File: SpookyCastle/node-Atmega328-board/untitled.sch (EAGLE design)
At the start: 20 parts, among them IC2 MEGA48/88/168-AU, J1 RJ11-6PTH

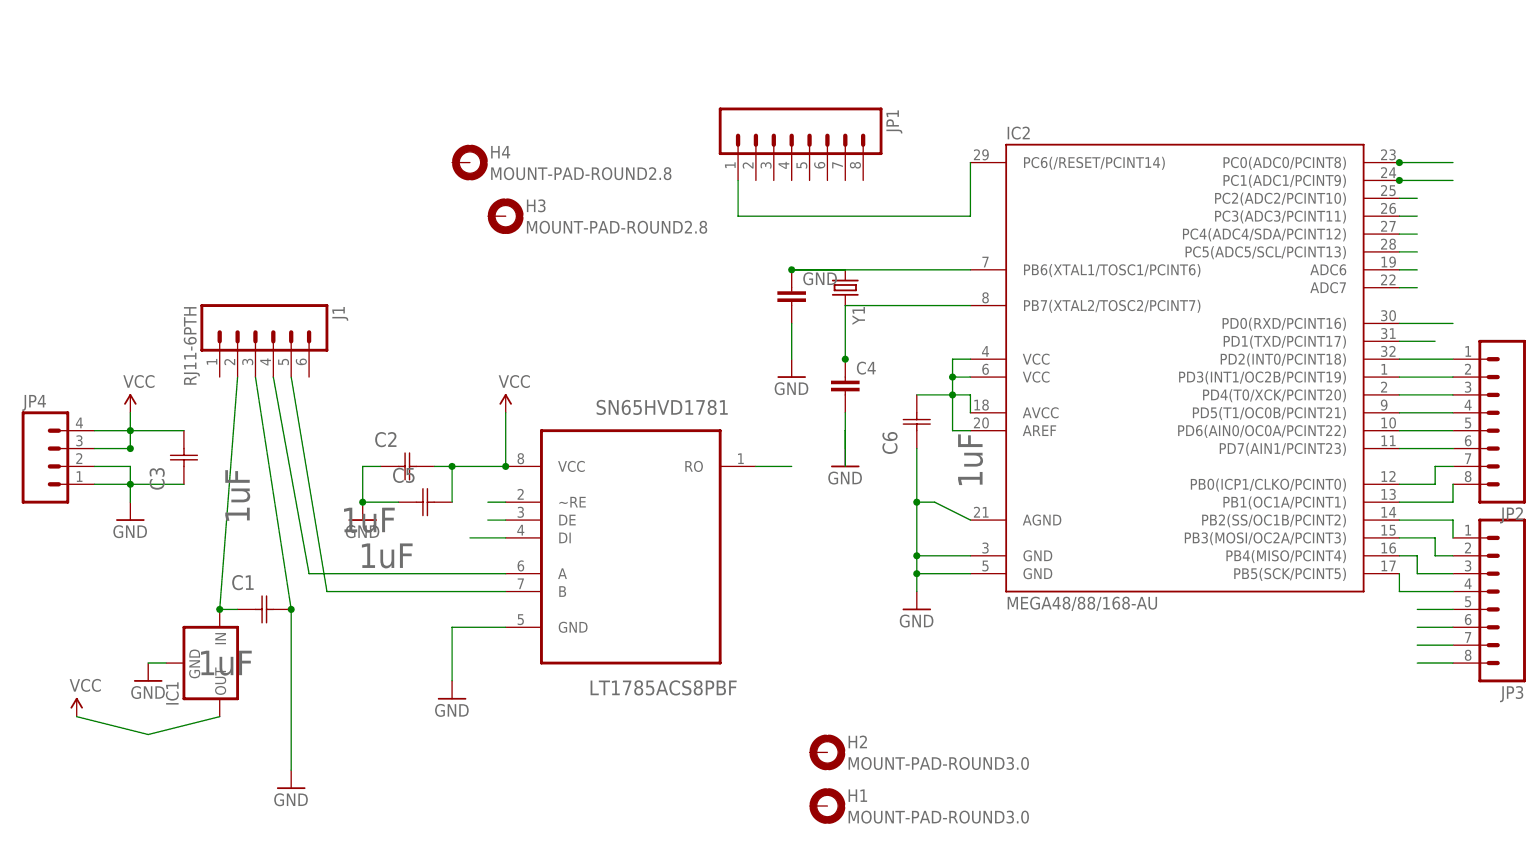
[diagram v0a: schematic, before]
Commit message: Almost finished with the SpookyCastle atmega board, core protocol version 0.7.6: Pin ordering changed for rs485, updated PDF.
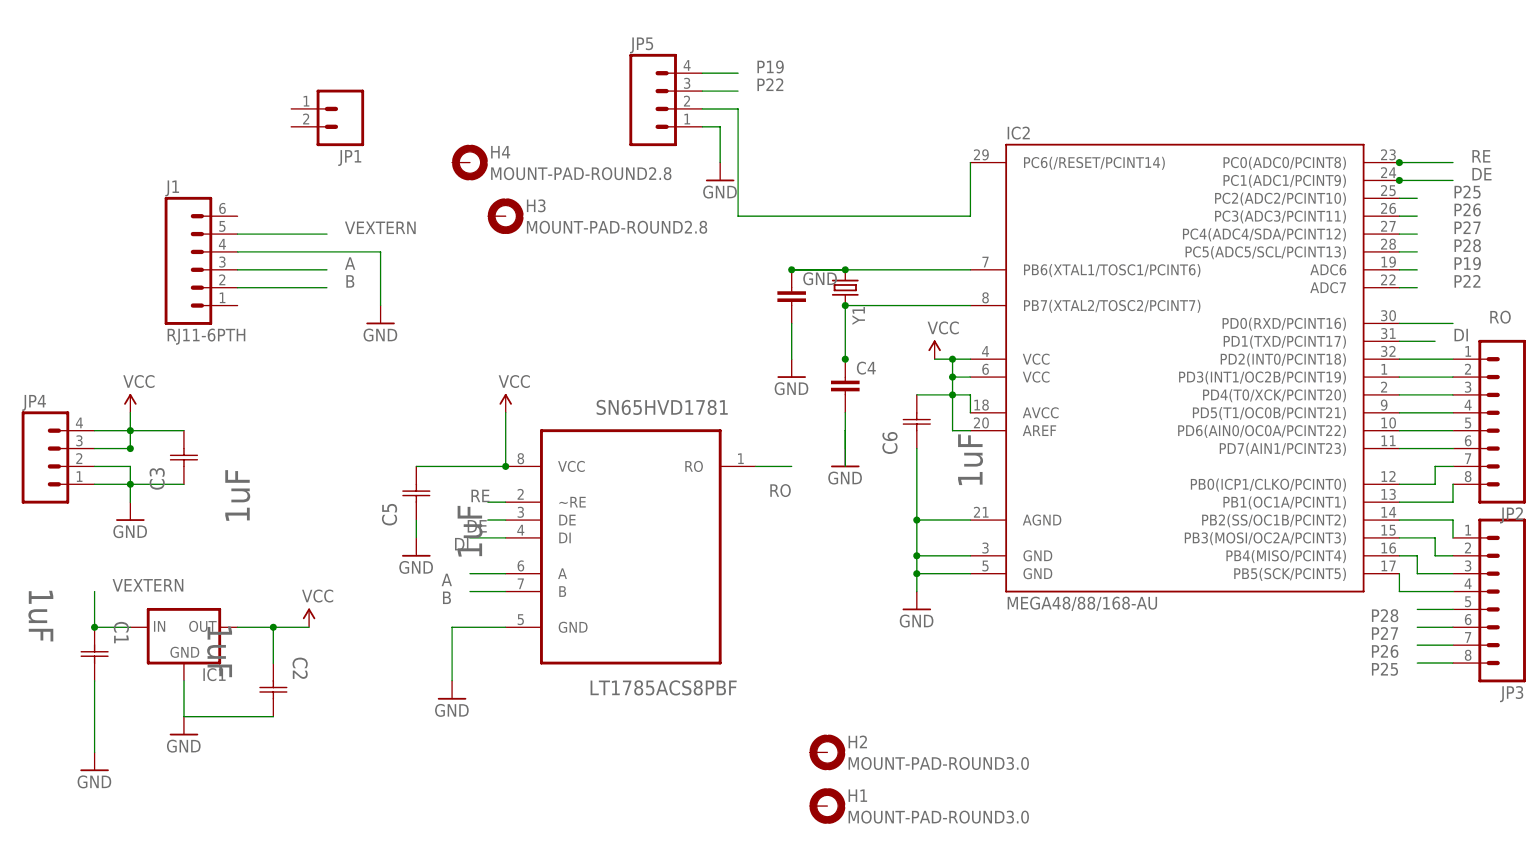
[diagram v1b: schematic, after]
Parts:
- added JP5: (no value), SparkFun - Copy:M04LOCK
- JP1: device SparkFun - Copy:M08LOCK -> SparkFun - Copy:M02PTH
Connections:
- removed net N$1: J1.4, SN65HVD1781.A
- removed net N$2: J1.5, SN65HVD1781.B
- removed net N$3: C1.C1, IC1.IN, J1.2
- new net A: J1.3, SN65HVD1781.A
- new net B: J1.2, SN65HVD1781.B
- new net VEXTERN: C1.C1, IC1.IN, J1.5
- net GND: now also C2.C2, J1.4, JP5.1; no longer C2.C1, J1.3
- net N$22: now also JP5.2; no longer JP1.1
- net P19: now also JP5.4
- net P22: now also JP5.3
- net VCC: now also C2.C1; no longer C2.C2
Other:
- moved on the sheet: C1, C2, C5, IC1, J1

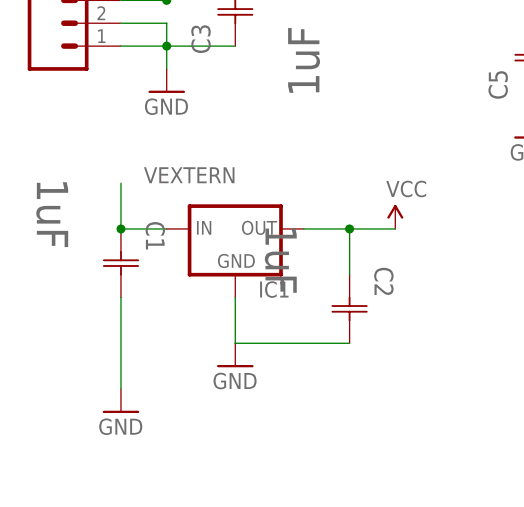
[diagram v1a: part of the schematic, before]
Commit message: Added option for 1210 capacitor on input of vreg, mitered some noise critical routing.
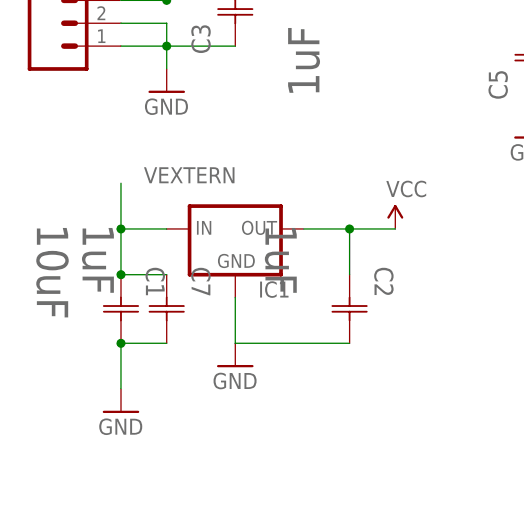
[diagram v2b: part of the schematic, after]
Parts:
- added C7: 1uF, Murata_By_element14_Batch_1:GRM21BR71H105KA12L
- C1: value 1uF -> 10uF; device Murata_By_element14_Batch_1:GRM21BR71H105KA12L -> Murata_By_element14_Batch_1:GRM32ER7YA106KA12L
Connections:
- net GND: now also C7.C2
- net VEXTERN: now also C7.C1
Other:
- moved on the sheet: C1
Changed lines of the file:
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@@
 <part name="GND1" library="SparkFun - Copy" deviceset="GND" device=""/>
 <part name="P+1" library="SparkFun - Copy" deviceset="VCC" device=""/>
-<part name="C1" library="Murata_By_element14_Batch_1" deviceset="GRM21BR71H105KA12L" device="" value="1uF"/>
 <part name="P+2" library="SparkFun - Copy" deviceset="VCC" device=""/>
 <part name="C2" library="Murata_By_element14_Batch_1" deviceset="GRM21BR71H105KA12L" device="" value="1uF"/>
@@
 <part name="JP5" library="SparkFun - Copy" deviceset="M04" device="LOCK"/>
 <part name="GND10" library="SparkFun - Copy" deviceset="GND" device=""/>
+<part name="C1" library="Murata_By_element14_Batch_1" deviceset="GRM32ER7YA106KA12L" device="" value="10uF"/>
+<part name="C7" library="Murata_By_element14_Batch_1" deviceset="GRM21BR71H105KA12L" device="" value="1uF">
+<attribute name="MPN" value="GRM21BR71H105KA12L "/>
+<attribute name="OC_FARNELL" value="1735541"/>
+<attribute name="OC_NEWARK" value="24R6342"/>
+<attribute name="SUPPLIER" value="Murata"/>
+<attribute name="TOLERANCE" value="±10%"/>
+<attribute name="VALUE" value="1uF"/>
+<attribute name="VOLTAGERATING" value="50V"/>
+</part>
 </parts>
 <sheets>
@@
 <instance part="GND1" gate="1" x="-15.24" y="15.24"/>
 <instance part="P+1" gate="1" x="15.24" y="35.56"/>
-<instance part="C1" gate="A" x="-15.24" y="35.56" rot="R270"/>
 <instance part="P+2" gate="1" x="43.18" y="66.04"/>
 <instance part="C2" gate="A" x="10.16" y="30.48" rot="R270"/>
@@
 <instance part="JP5" gate="G$1" x="66.04" y="109.22"/>
 <instance part="GND10" gate="1" x="73.66" y="99.06"/>
+<instance part="C1" gate="A" x="-15.24" y="30.48" rot="R270"/>
+<instance part="C7" gate="A" x="-10.16" y="30.48" rot="R270"/>
 </instances>
 <busses>
@@
 </segment>
 <segment>
-<wire x1="-15.24" y1="27.94" x2="-15.24" y2="17.78" width="0.1524" layer="91"/>
-<pinref part="GND1" gate="1" pin="GND"/>
-<pinref part="C1" gate="A" pin="C2"/>
-</segment>
-<segment>
 <pinref part="C4" gate="G$1" pin="2"/>
 <pinref part="GND4" gate="1" pin="GND"/>
@@
 <pinref part="GND10" gate="1" pin="GND"/>
 </segment>
+<segment>
+<pinref part="GND1" gate="1" pin="GND"/>
+<pinref part="C1" gate="A" pin="C2"/>
+<wire x1="-15.24" y1="17.78" x2="-15.24" y2="22.86" width="0.1524" layer="91"/>
+<pinref part="C7" gate="A" pin="C2"/>
+<wire x1="-10.16" y1="22.86" x2="-15.24" y2="22.86" width="0.1524" layer="91"/>
+<junction x="-15.24" y="22.86"/>
+</segment>
 </net>
 <net name="VEXTERN" class="1">
 <segment>
-<pinref part="C1" gate="A" pin="C1"/>
 <pinref part="IC1" gate="G$1" pin="IN"/>
 <wire x1="-10.16" y1="35.56" x2="-15.24" y2="35.56" width="0.1524" layer="91"/>
-<junction x="-15.24" y="35.56"/>
 <wire x1="-15.24" y1="35.56" x2="-15.24" y2="40.64" width="0.1524" layer="91"/>
 <label x="-12.7" y="40.64" size="1.778" layer="95"/>
-</segment>
-<segment>
+<pinref part="C1" gate="A" pin="C1"/>
+<wire x1="-15.24" y1="30.48" x2="-15.24" y2="35.56" width="0.1524" layer="91"/>
+<junction x="-15.24" y="35.56"/>
+<pinref part="C7" gate="A" pin="C1"/>
+<wire x1="-15.24" y1="30.48" x2="-10.16" y2="30.48" width="0.1524" layer="91"/>
+<junction x="-15.24" y="30.48"/>
+</segment>
+<segment>

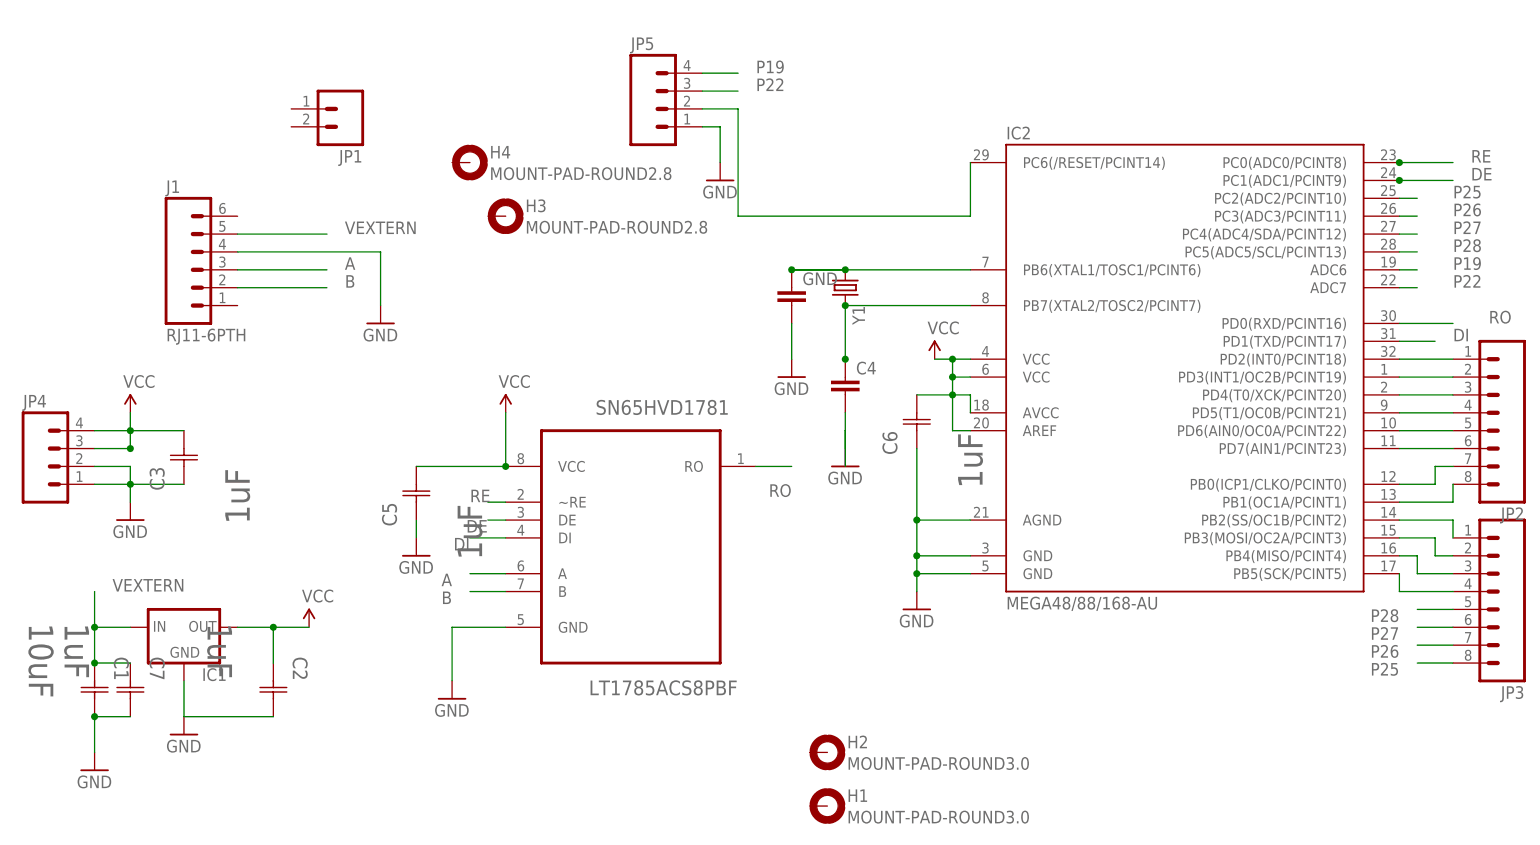
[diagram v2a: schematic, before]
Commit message: Added option for bigger capacitor.
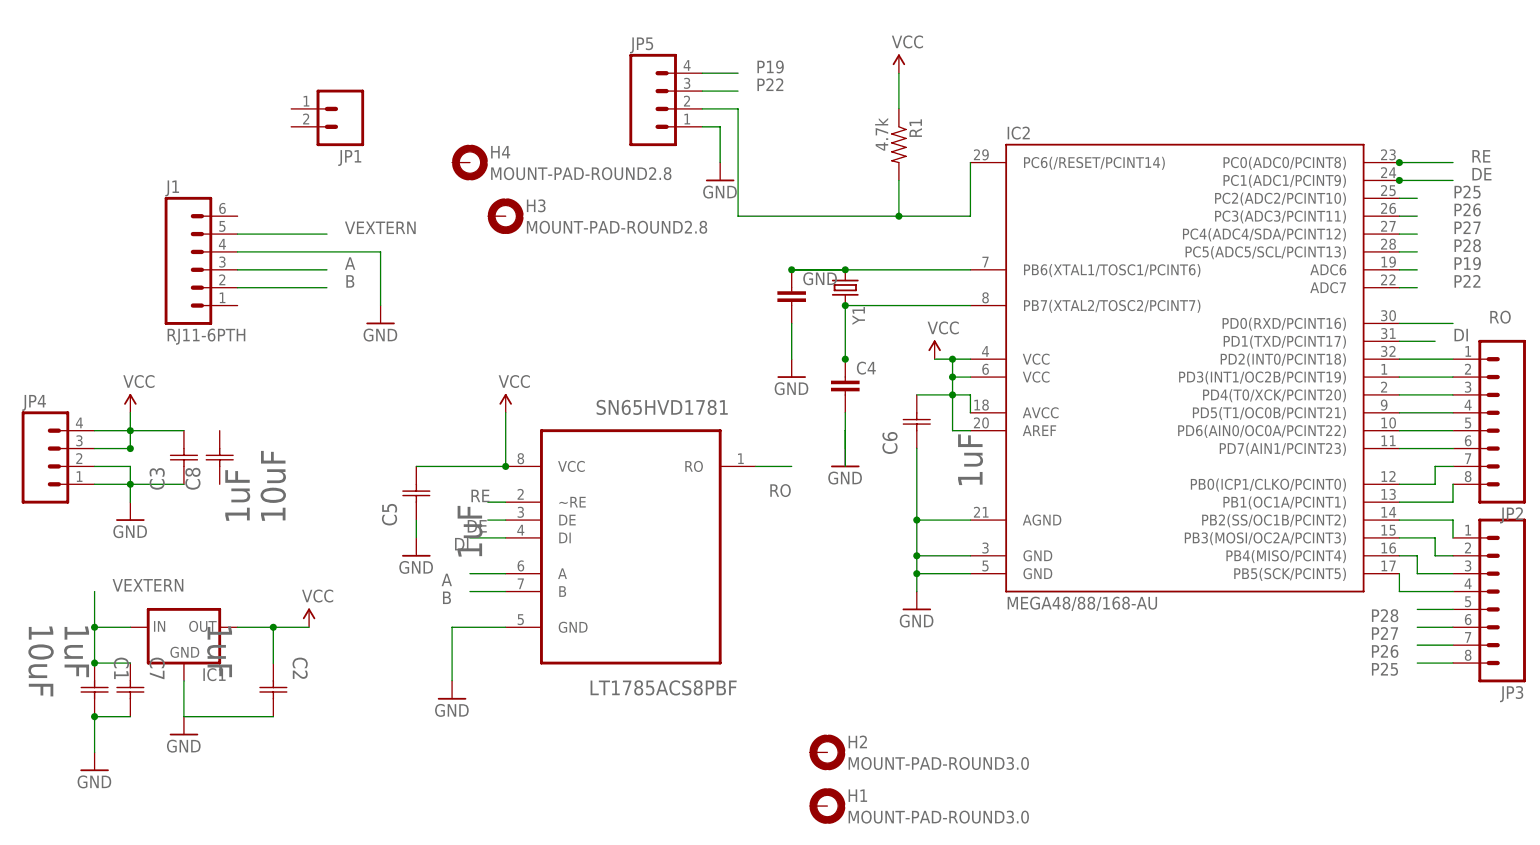
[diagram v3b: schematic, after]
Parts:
- added C8: 10uF, Murata_By_element14_Batch_1:GRM32ER7YA106KA12L
- added R1: 4.7k, SparkFun - Copy:RESISTOR0805-RES
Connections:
- net N$22: now also R1.2
- net VCC: now also R1.1
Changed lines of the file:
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@@
 <attribute name="VOLTAGERATING" value="50V"/>
+</part>
+<part name="R1" library="SparkFun - Copy" deviceset="RESISTOR" device="0805-RES" value="4.7k"/>
+<part name="P+5" library="SparkFun - Copy" deviceset="VCC" device=""/>
+<part name="C8" library="Murata_By_element14_Batch_1" deviceset="GRM32ER7YA106KA12L" device="" value="10uF">
+<attribute name="MPN" value="GRM32ER7YA106KA12L"/>
+<attribute name="OC_FARNELL" value="1735537"/>
+<attribute name="OC_NEWARK" value="24R2634"/>
+<attribute name="SUPPLIER" value="Murata"/>
+<attribute name="TOLERANCE" value="±10%"/>
+<attribute name="VALUE" value="10uF"/>
+<attribute name="VOLTAGERATING" value="35V"/>
 </part>
 </parts>
@@
 <instance part="C1" gate="A" x="-15.24" y="30.48" rot="R270"/>
 <instance part="C7" gate="A" x="-10.16" y="30.48" rot="R270"/>
+<instance part="R1" gate="G$1" x="99.06" y="104.14" rot="R270"/>
+<instance part="P+5" gate="1" x="99.06" y="114.3"/>
+<instance part="C8" gate="A" x="2.54" y="55.88" rot="R90"/>
 </instances>
 <busses>
@@
 <wire x1="-10.16" y1="63.5" x2="-2.54" y2="63.5" width="0.1524" layer="91"/>
 </segment>
+<segment>
+<pinref part="R1" gate="G$1" pin="1"/>
+<pinref part="P+5" gate="1" pin="VCC"/>
+<wire x1="99.06" y1="109.22" x2="99.06" y2="114.3" width="0.1524" layer="91"/>
+</segment>
 </net>
 <net name="RO" class="0">
@@
 <net name="N$22" class="0">
 <segment>
-<wire x1="76.2" y1="93.98" x2="109.22" y2="93.98" width="0.1524" layer="91"/>
+<wire x1="76.2" y1="93.98" x2="99.06" y2="93.98" width="0.1524" layer="91"/>
+<wire x1="99.06" y1="93.98" x2="109.22" y2="93.98" width="0.1524" layer="91"/>
 <wire x1="109.22" y1="93.98" x2="109.22" y2="101.6" width="0.1524" layer="91"/>
 <pinref part="IC2" gate="1" pin="PC6(/RESET/PCINT14)"/>
@@
 <pinref part="JP5" gate="G$1" pin="2"/>
 <wire x1="76.2" y1="109.22" x2="71.12" y2="109.22" width="0.1524" layer="91"/>
-</segment>
-</net>
+<pinref part="R1" gate="G$1" pin="2"/>
+<wire x1="99.06" y1="99.06" x2="99.06" y2="93.98" width="0.1524" layer="91"/>
+<junction x="99.06" y="93.98"/>
+</segment>
+</net>
